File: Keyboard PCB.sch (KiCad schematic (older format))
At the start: 150 parts, among them SW1 SW_Push, U1 ATmega32U4-AU, Y1 16MHz

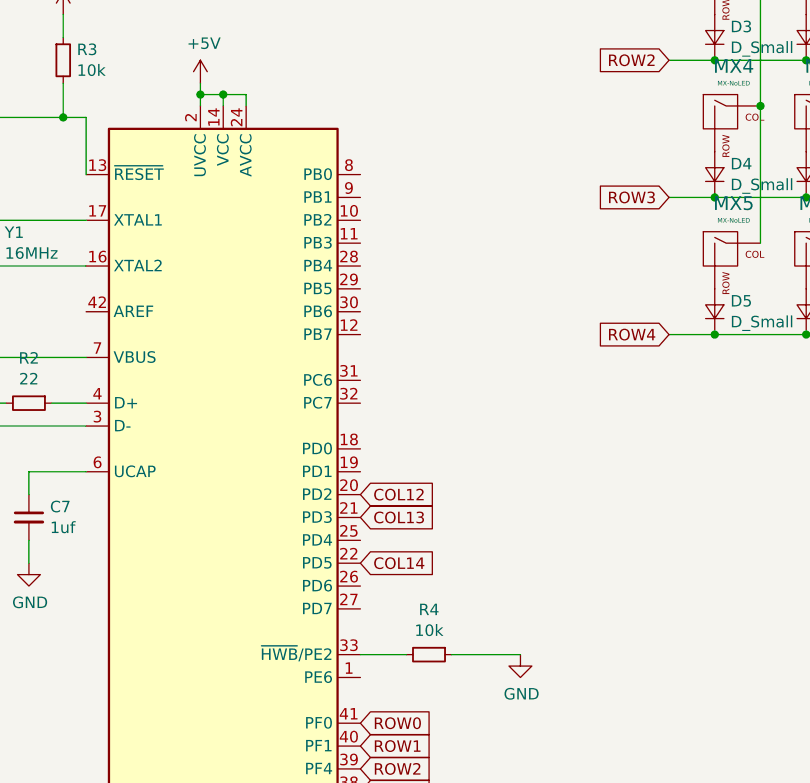
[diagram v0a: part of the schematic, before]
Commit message: 1st routing completion
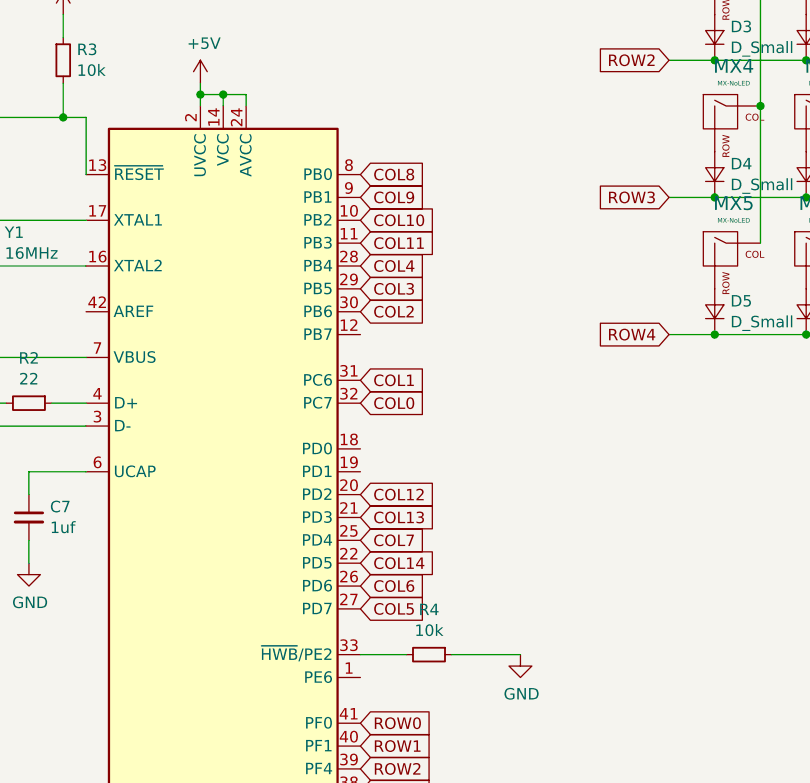
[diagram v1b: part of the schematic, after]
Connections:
- net COL0: now also U1.32 (PC7)
- net COL1: now also U1.31 (PC6)
- net COL10: now also U1.10 (PB2)
- net COL11: now also U1.11 (PB3)
- net COL2: now also U1.30 (PB6)
- net COL3: now also U1.29 (PB5)
- net COL4: now also U1.28 (PB4)
- net COL5: now also U1.27 (PD7)
- net COL6: now also U1.26 (PD6)
- net COL7: now also U1.25 (PD4)
- net COL8: now also U1.8 (PB0)
- net COL9: now also U1.9 (PB1)
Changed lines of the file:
@@
 Text GLabel 3100 5100 2    50   Input ~ 0
 COL12
+Text GLabel 3100 4000 2    50   Input ~ 0
+COL11
+Text GLabel 3100 3900 2    50   Input ~ 0
+COL10
+Text GLabel 3100 3800 2    50   Input ~ 0
+COL9
+Text GLabel 3100 3700 2    50   Input ~ 0
+COL8
+Text GLabel 3100 5300 2    50   Input ~ 0
+COL7
+Text GLabel 3100 5500 2    50   Input ~ 0
+COL6
+Text GLabel 3100 5600 2    50   Input ~ 0
+COL5
+Text GLabel 3100 4700 2    50   Input ~ 0
+COL0
+Text GLabel 3100 4600 2    50   Input ~ 0
+COL1
+Text GLabel 3100 4300 2    50   Input ~ 0
+COL2
+Text GLabel 3100 4200 2    50   Input ~ 0
+COL3
+Text GLabel 3100 4100 2    50   Input ~ 0
+COL4
 $EndSCHEMATC

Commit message: fixes
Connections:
- net COL0: now also U1.28 (PB4); no longer U1.32 (PC7)
- net COL1: now also U1.29 (PB5); no longer U1.31 (PC6)
- net COL3: now also U1.31 (PC6); no longer U1.29 (PB5)
- net COL4: now also U1.32 (PC7); no longer U1.28 (PB4)
- net COL5: now also U1.25 (PD4); no longer U1.27 (PD7)
- net COL7: now also U1.27 (PD7); no longer U1.25 (PD4)
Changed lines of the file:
@@
 Text GLabel 3100 3700 2    50   Input ~ 0
 COL8
-Text GLabel 3100 5300 2    50   Input ~ 0
+Text GLabel 3100 5600 2    50   Input ~ 0
 COL7
 Text GLabel 3100 5500 2    50   Input ~ 0
 COL6
-Text GLabel 3100 5600 2    50   Input ~ 0
+Text GLabel 3100 5300 2    50   Input ~ 0
 COL5
-Text GLabel 3100 4700 2    50   Input ~ 0
+Text GLabel 3100 4100 2    50   Input ~ 0
 COL0
-Text GLabel 3100 4600 2    50   Input ~ 0
+Text GLabel 3100 4200 2    50   Input ~ 0
 COL1
 Text GLabel 3100 4300 2    50   Input ~ 0
 COL2
-Text GLabel 3100 4200 2    50   Input ~ 0
+Text GLabel 3100 4600 2    50   Input ~ 0
 COL3
-Text GLabel 3100 4100 2    50   Input ~ 0
+Text GLabel 3100 4700 2    50   Input ~ 0
 COL4
 $EndSCHEMATC

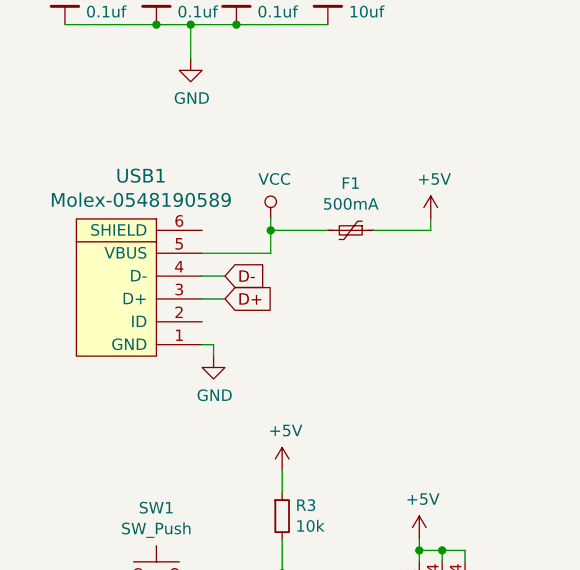
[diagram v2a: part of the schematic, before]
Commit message: Add submodules
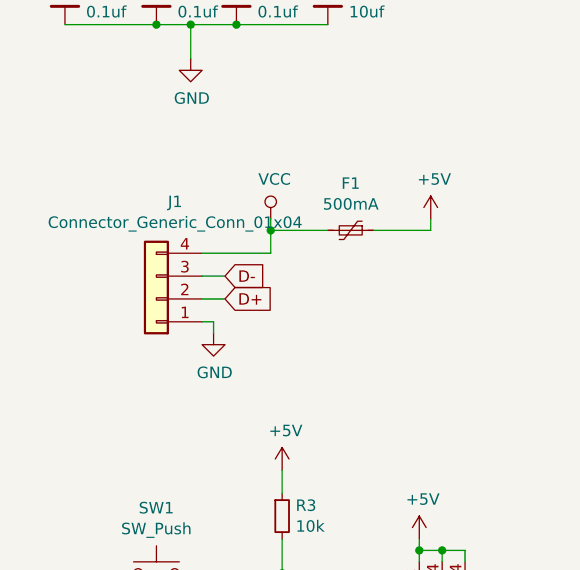
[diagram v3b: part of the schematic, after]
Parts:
- removed USB1: Molex-0548190589, random-keyboard-parts:Molex-0548190589, symbol random-keyboard-parts:Molex-0548190589
- added J1: Connector_Generic_Conn_01x04, Connector_JST:JST_ZE_SM04B-ZESS-TB_1x04-1MP_P1.50mm_Horizontal, symbol Unified-Daughterboard-cache:Connector_Generic_Conn_01x04
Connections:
- net D+: now also J1.2 (Pin_2)
- net D-: now also J1.3 (Pin_3)
- net GND: now also J1.1 (Pin_1)
- net VCC: now also J1.4 (Pin_4)
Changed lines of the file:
@@
 	900  4700 1550 4700
-$Comp
-L random-keyboard-parts:Molex-0548190589 USB1
-U 1 1 5E4525DF
-P 1150 2250
-F 0 "USB1" V 1687 2217 60  0000 C CNN
-F 1 "Molex-0548190589" V 1581 2217 60  0000 C CNN
-F 2 "random-keyboard-parts:Molex-0548190589" H 1150 2250 60  0001 C CNN
-F 3 "" H 1150 2250 60  0001 C CNN
-	1    1150 2250
-	0    -1   -1   0
-$EndComp
 $Comp
 L power:VCC #PWR0111
@@
 L power:GND #PWR0113
 U 1 1 5E462233
-P 1500 2500
-F 0 "#PWR0113" H 1500 2250 50  0001 C CNN
-F 1 "GND" H 1505 2327 50  0000 C CNN
-F 2 "" H 1500 2500 50  0001 C CNN
-F 3 "" H 1500 2500 50  0001 C CNN
-	1    1500 2500
-	1    0    0    -1
-$EndComp
-Wire Wire Line
-	1500 2500 1500 2450
-Wire Wire Line
-	1500 2450 1450 2450
+P 1500 2400
+F 0 "#PWR0113" H 1500 2150 50  0001 C CNN
+F 1 "GND" H 1505 2227 50  0000 C CNN
+F 2 "" H 1500 2400 50  0001 C CNN
+F 3 "" H 1500 2400 50  0001 C CNN
+	1    1500 2400
+	1    0    0    -1
+$EndComp
+Wire Wire Line
+	1500 2400 1500 2350
+Wire Wire Line
+	1500 2350 1450 2350
 Text GLabel 1550 2150 2    50   Input ~ 0
 D-
@@
 Text GLabel 3100 4700 2    50   Input ~ 0
 COL4
+$Comp
+L Unified-Daughterboard-cache:Connector_Generic_Conn_01x04 J1
+U 1 1 5E4C585F
+P 1250 2250
+F 0 "J1" H 1168 1825 50  0000 C CNN
+F 1 "Connector_Generic_Conn_01x04" H 1168 1916 50  0000 C CNN
+F 2 "Connector_JST:JST_ZE_SM04B-ZESS-TB_1x04-1MP_P1.50mm_Horizontal" H 1250 2250 50  0001 C CNN
+F 3 "" H 1250 2250 50  0001 C CNN
+	1    1250 2250
+	-1   0    0    1
+$EndComp
 $EndSCHEMATC

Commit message: Final keyboard file extraction
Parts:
- removed F1: 500mA, Fuse:Fuse_1206_3216Metric_Pad1.42x1.75mm_HandSolder, symbol Device:Polyfuse_Small
- removed J1: Connector_Generic_Conn_01x04, Connector_JST:JST_ZE_SM04B-ZESS-TB_1x04-1MP_P1.50mm_Horizontal, symbol Unified-Daughterboard-cache:Connector_Generic_Conn_01x04
- added R5, R6: 5.1k, Resistor_SMD:R_0805_2012Metric_Pad1.15x1.40mm_HandSolder, symbol Device:R_Small
- added USB1: Type-C_HRO-TYPE-C-31-M-12, Type-C:HRO-TYPE-C-31-M-12-HandSoldering, symbol Unified-Daughterboard-cache:Type-C_HRO-TYPE-C-31-M-12
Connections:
- net D+: now also USB1.6 (DP1), USB1.8 (DP2)
- net D-: now also USB1.5 (DN2), USB1.7 (DN1)
- net GND: now also R5.2, R6.2, USB1.1 (GND), USB1.12 (GND), USB1.13 (SHIELD)
- net VCC: now also USB1.11 (VBUS), USB1.2 (VBUS)
- new net: R5.1, USB1.10 (CC2)
- new net: R6.1, USB1.4 (CC1)
- no-connect marks 0 -> 2
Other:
- moved on the sheet: C1, C2, C3, C4, C5, C6, C7, D1, D10, D11, D12, D13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
